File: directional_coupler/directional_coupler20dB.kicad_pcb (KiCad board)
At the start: 2 copper layers, 16 parts, among them U1 SMA_PCB_Edge_Mount, U2 SMA_PCB_Edge_Mount, U3 SMA_PCB_Edge_Mount, U4 SMA_PCB_Edge_Mount

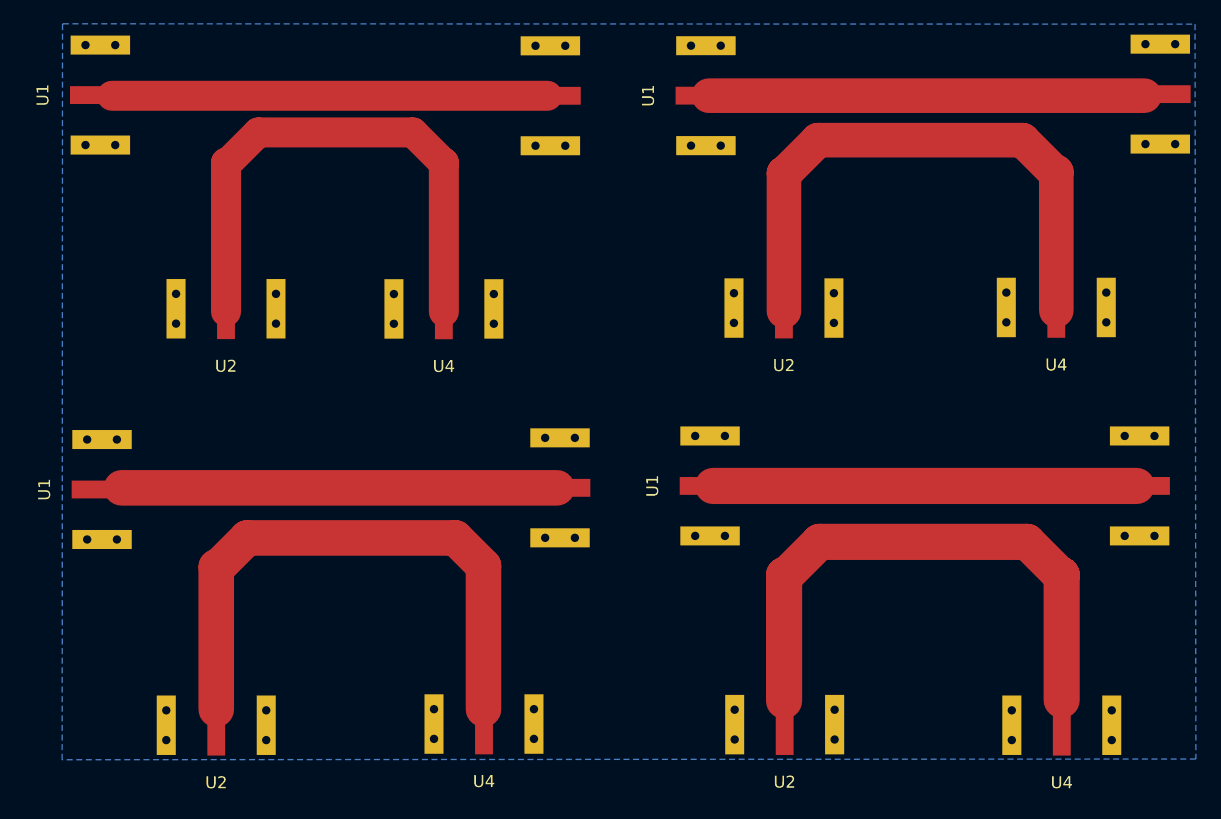
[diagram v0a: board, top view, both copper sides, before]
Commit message: Fixed some silkscreen, put SMA connector pads closer to the edges
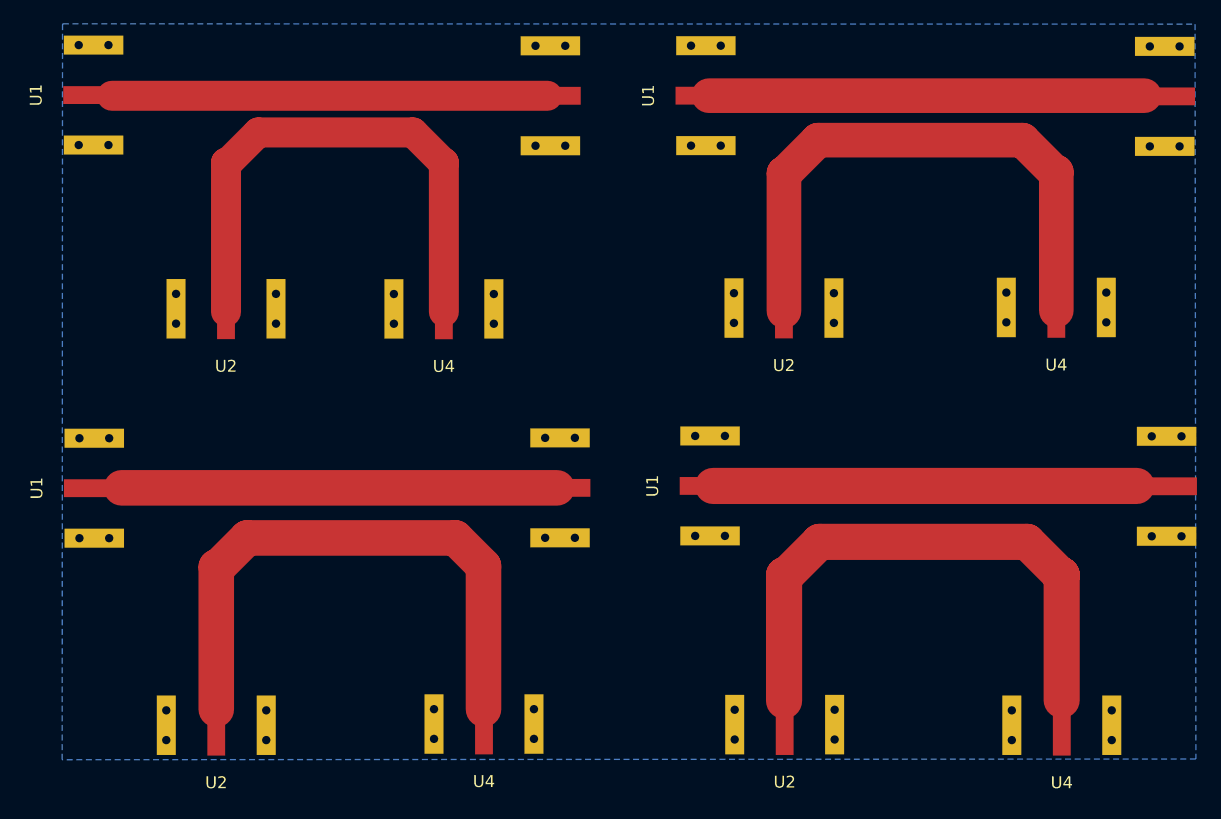
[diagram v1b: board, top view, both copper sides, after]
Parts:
- moved U3 2.27 mm to (158.4, 136.1)
- moved U1 0.66 mm to (68.8, 136.3)
- moved U1 0.57 mm to (68.8, 103.2)
- moved U3 0.42 mm to (158.3, 103.3)
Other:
- board text added: "-14 dB Directional Coupler Husky Satellite Lab Designed by Katharine Lundblad"
- board text added: "-16 dB Directional Coupler Husky Satellite Lab Designed by Katharine Lundblad"
- board text added: "-18 dB Directional Coupler Husky Satellite Lab Designed by Katharine Lundblad"
- board text added: "-20 dB Directional Coupler Husky Satellite Lab Designed by Katharine Lundblad"
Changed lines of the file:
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@@
   (general
     (thickness 1.6)
-    (drawings 10)
+    (drawings 14)
     (tracks 34)
     (zones 0)
@@
   )
   (setup
-    (last_trace_width 2.52159)
+    (last_trace_width 0.25)
     (user_trace_width 2.52159)
     (user_trace_width 2.91102)
@@
       (psa4output false)
       (plotreference true)
-      (plotvalue false)
+      (plotvalue true)
       (plotinvisibletext false)
       (padsonsilk false)
@@
   )
   (module HS2_parts:SMA_EDGE_MOUNT_132255 (layer F.Cu)
-    (at 69.46 136.37 270)
+    (at 68.81 136.26 270)
     (fp_text reference U1 (at 0 5.08 90) (layer F.SilkS)
       (effects (font (size 1 1) (thickness 0.15)))
@@
   )
   (module HS2_parts:SMA_EDGE_MOUNT_132255 (layer F.Cu)
-    (at 156.16 136.07 90)
+    (at 158.43 136.1 90)
     (fp_text reference U3 (at 0 5.08 90) (layer F.SilkS) hide
       (effects (font (size 1 1) (thickness 0.15)))
@@
   )
   (module HS2_parts:SMA_EDGE_MOUNT_132255 (layer F.Cu)
-    (at 157.9 103.14 90)
+    (at 158.27 103.33 90)
     (fp_text reference U3 (at 0 5.08 90) (layer F.SilkS) hide
       (effects (font (size 1 1) (thickness 0.15)))
@@
   )
   (module HS2_parts:SMA_EDGE_MOUNT_132255 (layer F.Cu)
-    (at 69.32 103.22 270)
+    (at 68.75 103.22 270)
     (fp_text reference U1 (at 0 5.08 90) (layer F.SilkS)
       (effects (font (size 1 1) (thickness 0.15)))
@@
       (net 1 GND))
   )
+  (gr_text "-16 dB Directional Coupler\nHusky Satellite Lab \nDesigned by Katharine Lundblad" (at 88.68 145.02) (layer B.SilkS)
+    (effects (font (size 1 1) (thickness 0.15)) (justify mirror))
+  )
+  (gr_text "-18 dB Directional Coupler\nHusky Satellite Lab \nDesigned by Katharine Lundblad" (at 137.27 144.67) (layer B.SilkS)
+    (effects (font (size 1 1) (thickness 0.15)) (justify mirror))
+  )
+  (gr_text "-14 dB Directional Coupler\nHusky Satellite Lab \nDesigned by Katharine Lundblad" (at 137.15 110.88) (layer B.SilkS)
+    (effects (font (size 1 1) (thickness 0.15)) (justify mirror))
+  )
+  (gr_text "-20 dB Directional Coupler\nHusky Satellite Lab\nDesigned by Katharine Lundblad" (at 88.33 111.12) (layer B.SilkS)
+    (effects (font (size 1 1) (thickness 0.15)) (justify mirror))
+  )
   (gr_line (start 65.17 159.69) (end 65.17 96.71) (layer Dwgs.User) (width 0.15))
